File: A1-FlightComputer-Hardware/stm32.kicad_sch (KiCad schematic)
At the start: 47 parts, among them J201 Conn_01x01_Socket, J202 Conn_01x01_Socket, J203 Conn_01x02_Socket, J204 Conn_01x02_Socket, J205 Conn_02x05_Odd_Even, SW201 SW_Push, SW202 SW_Push, SW203 SW_SPDT, U201 STM32L475RCTx, U202 W25N01GVZEIG, Y201 32.768kHz LSE, Y202 8MHz HSE

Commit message: Flight computer V2
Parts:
- removed J201, J202: Conn_01x01_Socket, Connector_PinSocket_2.54mm:PinSocket_1x01_P2.54mm_Vertical, symbol Connector:Conn_01x01_Socket
- removed JP201, JP202: SolderJumper_2_Bridged, Jumper:SolderJumper-2_P1.3mm_Bridged_RoundedPad1.0x1.5mm, symbol Jumper:SolderJumper_2_Bridged
- removed TP202: ~, TestPoint:TestPoint_THTPad_D1.0mm_Drill0.5mm, symbol Connector:TestPoint
- R202: DK_Number 311-10KLDCT-ND -> 311-1KLDCT-ND
- renumbered JP203 to JP201, JP204 to JP202, TP203 to TP202, TP204 to TP203, TP205 to TP204, TP206 to TP205, TP207 to TP206, TP208 to TP207, TP209 to TP208
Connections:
- net Actuator_IN1: no longer names the net of U201.61 (PB8)
- net Actuator_IN2: no longer names the net of U201.62 (PB9)
- net GoPro_ON renamed Buzzer_ON
- net PB15: no longer names the net of U201.36 (PB15)
- net PC12: no longer names the net of U201.53 (PC12)
- net Payload_TEMP: no longer names the net of U201.28 (PB2)
- net STG0: no longer names the net of U201.17 (PA3)
- net STG1: no longer names the net of U201.16 (PA2)
- net STG2: no longer names the net of U201.15 (PA1)
- net STG3: no longer names the net of U201.14 (PA0)
- no-connect marks 1 -> 11

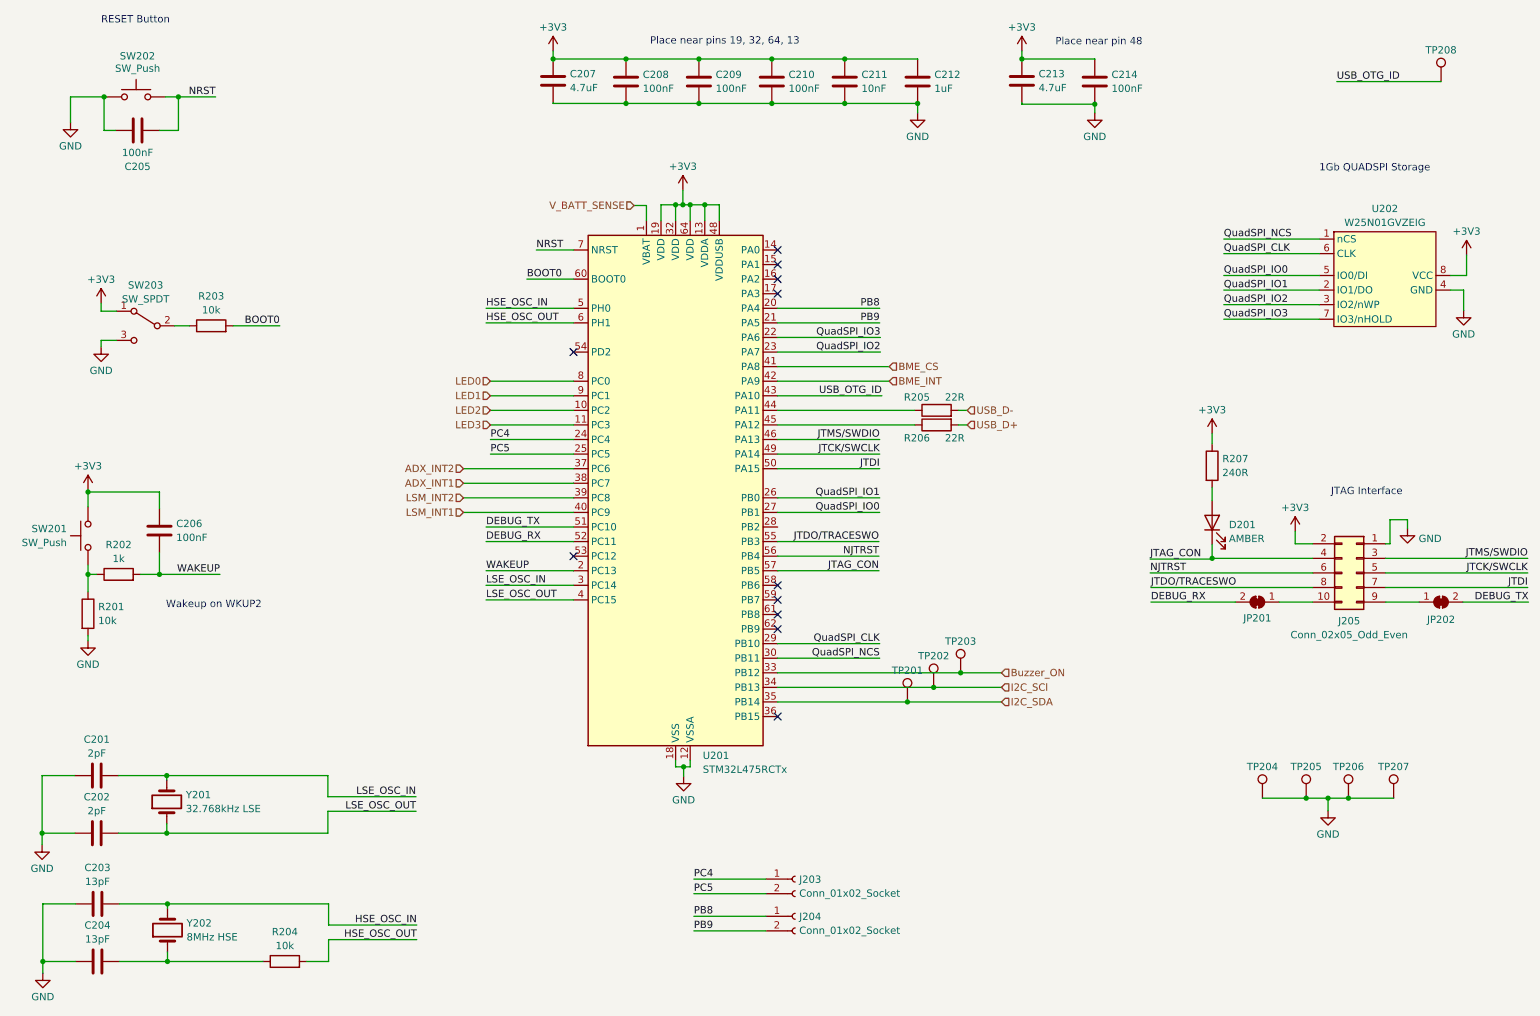
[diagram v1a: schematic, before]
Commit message: Added voltage divider and connected BATT+ to ADC pin, spaced out battery and switch ports
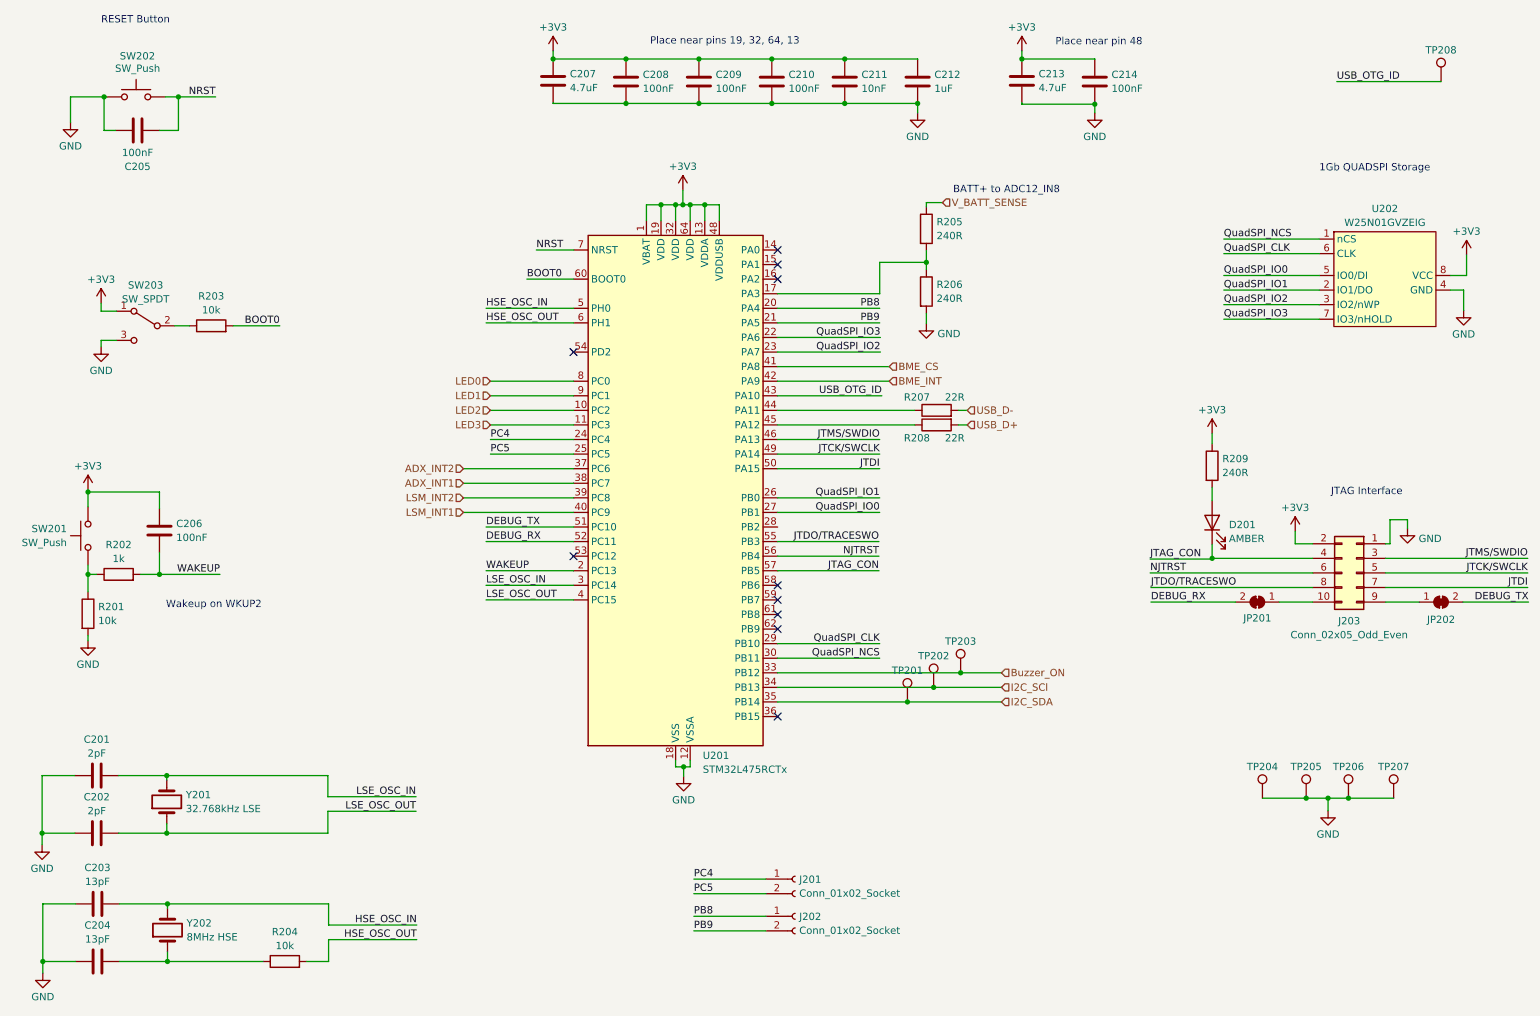
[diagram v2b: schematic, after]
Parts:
- added R205, R206: 240R, Resistor_SMD:R_0603_1608Metric_Pad0.98x0.95mm_HandSolder, symbol Device:R
- renumbered J203 to J201, J204 to J202, J205 to J203, R205 to R207, R206 to R208, R207 to R209
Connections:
- net +3V3: now also U201.1 (VBAT)
- net GND: now also R206.2
- net V_BATT_SENSE: now also R205.1; no longer U201.1 (VBAT)
- net at U201.17 (PA3): now also R205.2, R206.1
- no-connect marks 11 -> 10
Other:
- note added: "BATT+ to ADC12_IN8"
